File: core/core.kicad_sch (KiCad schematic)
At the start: 5 parts, among them U1 F1C200S, U2 EA3036C

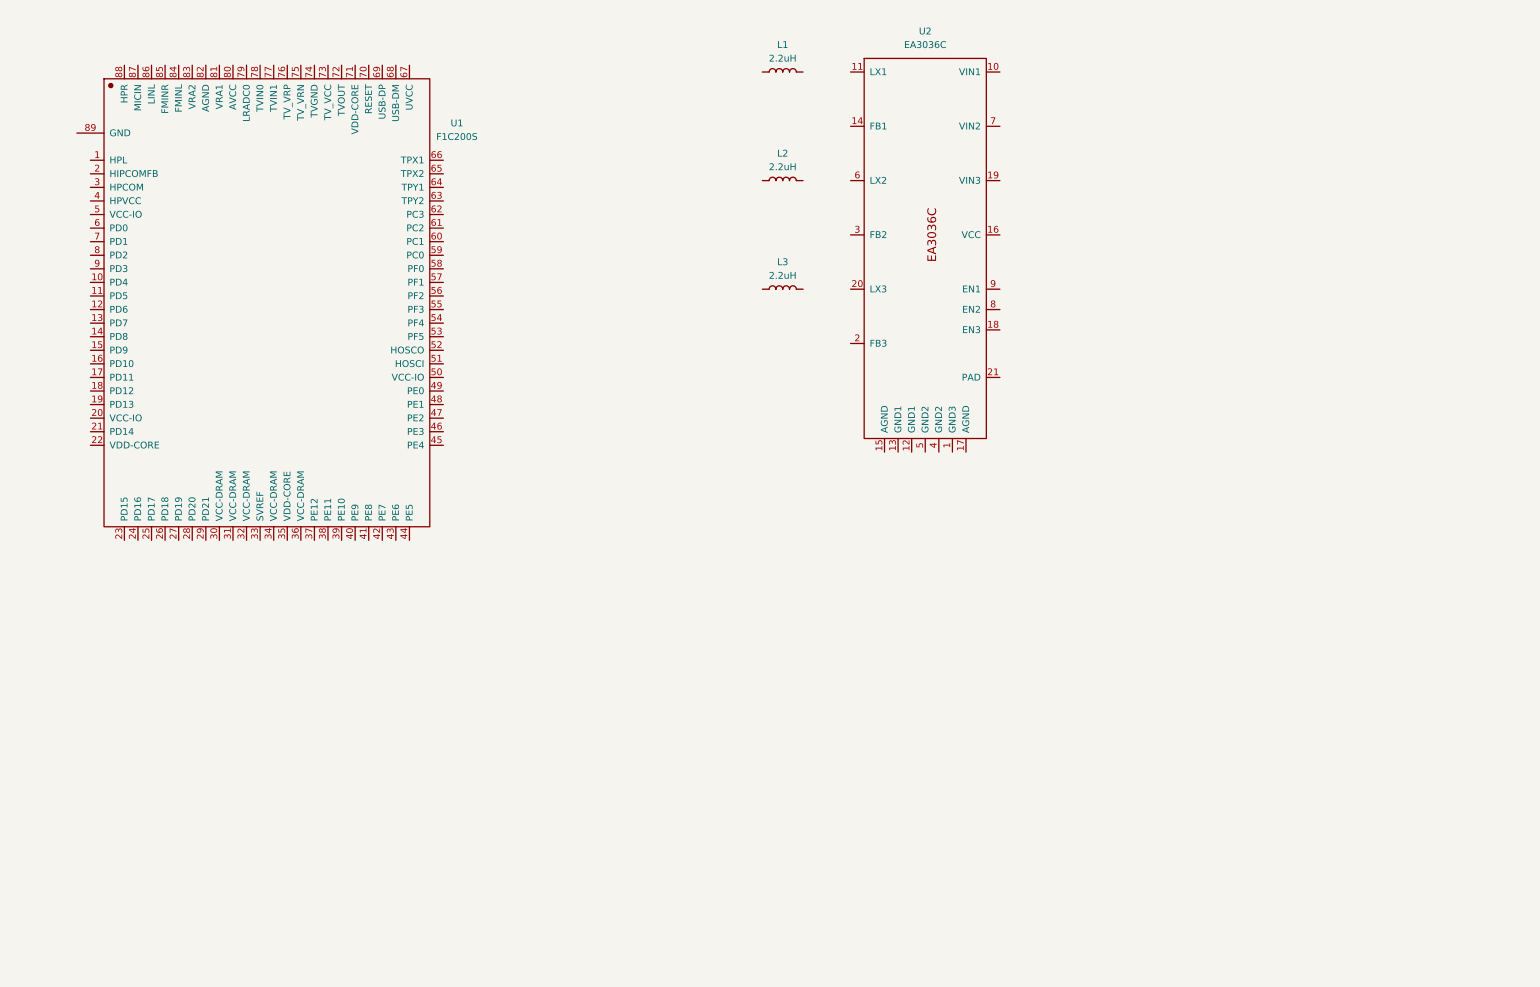
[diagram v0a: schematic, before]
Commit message: finish schemtic except soc
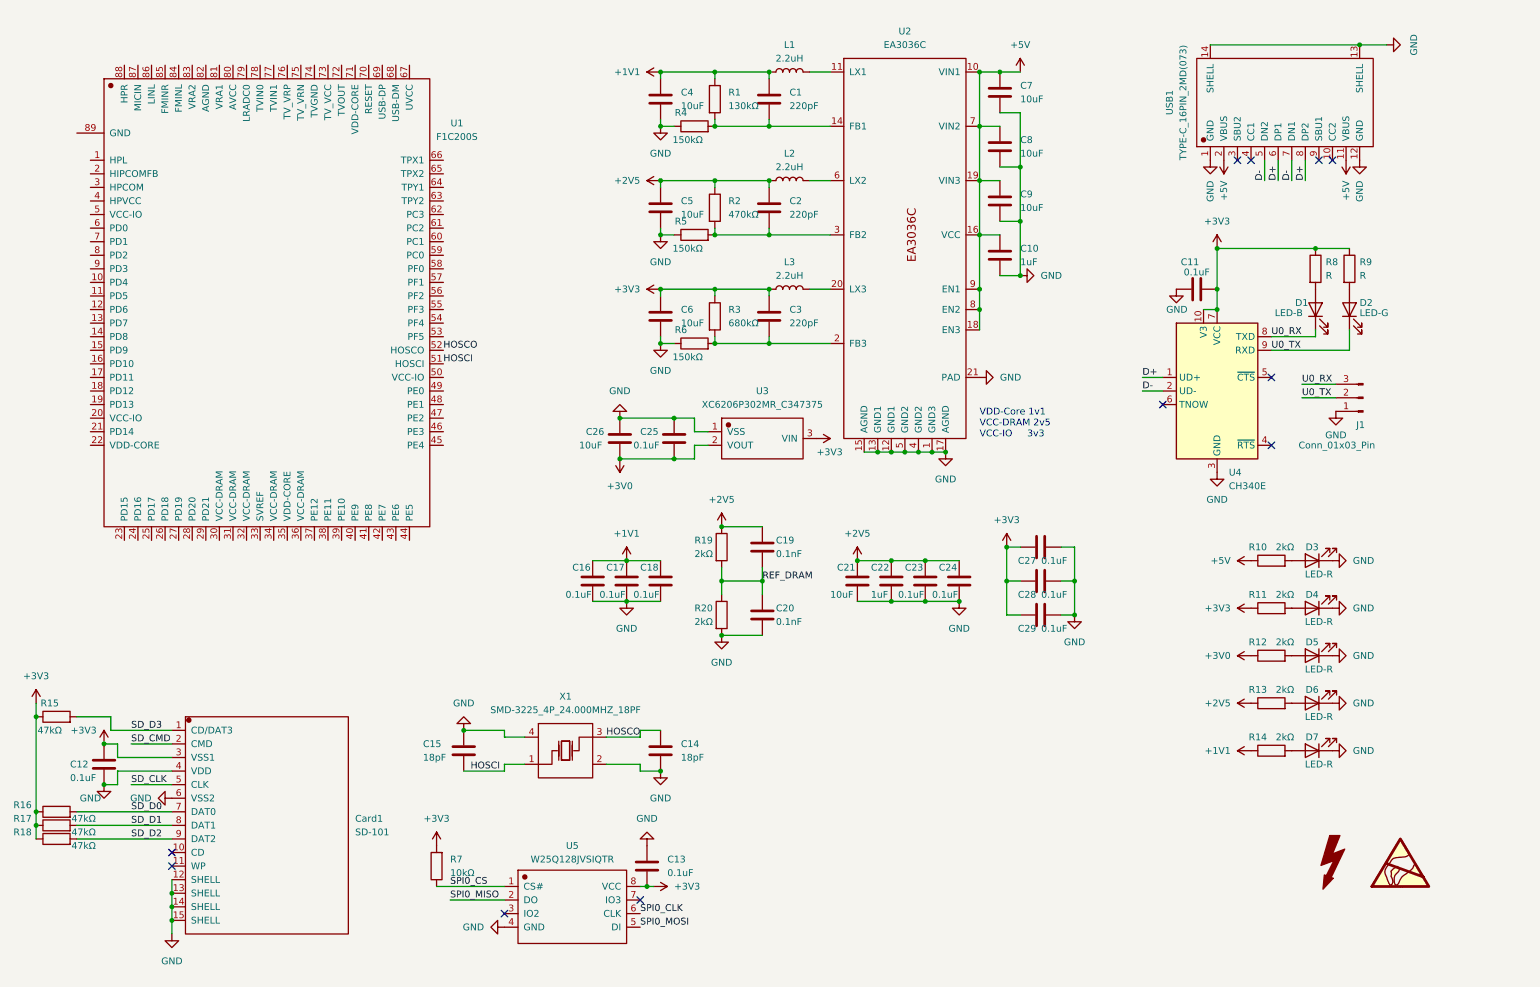
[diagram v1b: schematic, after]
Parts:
- added C1, C2, C3: 220pF, Capacitor_SMD:C_0603_1608Metric_Pad1.08x0.95mm_HandSolder, symbol Device:C
- added C10: 1uF, symbol Device:C
- added C11, C12, C13: 0.1uF, symbol Device:C
- added C14, C15: 18pF, symbol Device:C
- added C16, C17, C18, C23, C24, C25: 0.1uF, Capacitor_SMD:C_0603_1608Metric_Pad1.08x0.95mm_HandSolder, symbol Device:C
- added C19, C20: 0.1nF, Capacitor_SMD:C_0603_1608Metric_Pad1.08x0.95mm_HandSolder, symbol Device:C
- added C21, C26: 10uF, Capacitor_SMD:C_0603_1608Metric_Pad1.08x0.95mm_HandSolder, symbol Device:C
- added C22: 1uF, Capacitor_SMD:C_0603_1608Metric_Pad1.08x0.95mm_HandSolder, symbol Device:C
- added C27, C28, C29: 0.1uF, Capacitor_SMD:C_0603_1608Metric, symbol Device:C
- added C4, C5, C6: 10uF, Capacitor_SMD:C_0805_2012Metric_Pad1.18x1.45mm_HandSolder, symbol Device:C
- added C7, C8, C9: 10uF, symbol Device:C
- added Card1: SD-101, kicad_lceda:SD-SMD_SD-101, symbol kicad_lceda:SD-101
- added D1: LED-B, LED_SMD:LED_0603_1608Metric_Pad1.05x0.95mm_HandSolder, symbol Device:LED
- added D2: LED-G, LED_SMD:LED_0603_1608Metric_Pad1.05x0.95mm_HandSolder, symbol Device:LED
- added D3, D4, D5, D6, D7: LED-R, LED_SMD:LED_0603_1608Metric_Pad1.05x0.95mm_HandSolder, symbol Device:LED
- added J1: Conn_01x03_Pin, Connector_PinHeader_2.54mm:PinHeader_1x03_P2.54mm_Vertical, symbol Connector:Conn_01x03_Pin
- added R1: 130kΩ, Resistor_SMD:R_0201_0603Metric_Pad0.64x0.40mm_HandSolder, symbol Device:R
- added R10, R11, R12, R13, R14: 2kΩ, LED_SMD:LED_0603_1608Metric_Pad1.05x0.95mm_HandSolder, symbol Device:R
- added R15, R16, R17, R18: 47kΩ, Resistor_SMD:R_0603_1608Metric_Pad0.98x0.95mm_HandSolder, symbol Device:R
- added R19, R20: 2kΩ, Resistor_SMD:R_0603_1608Metric_Pad0.98x0.95mm_HandSolder, symbol Device:R
- added R2: 470kΩ, Resistor_SMD:R_0201_0603Metric_Pad0.64x0.40mm_HandSolder, symbol Device:R
- added R3: 680kΩ, Resistor_SMD:R_0201_0603Metric_Pad0.64x0.40mm_HandSolder, symbol Device:R
- added R4, R5, R6: 150kΩ, Resistor_SMD:R_0201_0603Metric_Pad0.64x0.40mm_HandSolder, symbol Device:R
- added R7: 10kΩ, symbol Device:R
- added R8, R9: R, symbol Device:R
- added U3: XC6206P302MR_C347375, kicad_lceda:SOT-23-3_L3.0-W1.7-P0.95-LS2.9-BR, symbol kicad_lceda:XC6206P302MR_C347375
- added U4: CH340E, Package_SO:MSOP-10_3x3mm_P0.5mm, symbol Interface_USB:CH340E
- added U5: W25Q128JVSIQTR, kicad_lceda:SOIC-8_L5.3-W5.3-P1.27-LS8.0-BL, symbol kicad_lceda:W25Q128JVSIQTR
- added USB1: TYPE-C_16PIN_2MD(073), kicad_lceda:USB-C-SMD_TYPE-C-6PIN-2MD-073, symbol kicad_lceda:TYPE-C_16PIN_2MD(073)
- added X1: SMD-3225_4P_24.000MHZ_18PF, kicad_lceda:CRYSTAL-SMD_4P-L3.2-W2.5-BL, symbol kicad_lceda:SMD-3225_4P_24.000MHZ_18PF
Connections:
- net GND: now reaches U2.1 (GND3)
- net GND: now also U2.12 (GND1), U2.13 (GND1), U2.15 (AGND), U2.17 (AGND), U2.21 (PAD), U2.4 (GND2), U2.5 (GND2), C10.2, C11.1, C12.1, C13.1, C14.2, C15.1, C16.2, C17.2, C18.2, C20.2, C21.2, C22.2, C23.2, C24.2, C25.1, C26.1, C27.2, C28.2, C29.2, C4.2, C5.2, C6.2, C7.2, C8.2, C9.2, Card1.12 (SHELL), Card1.13 (SHELL), Card1.14 (SHELL), Card1.15 (SHELL), Card1.4 (VDD), Card1.6 (VSS2), D3.1 (K), D4.1 (K), D5.1 (K), D6.1 (K), D7.1 (K), J1.1 (Pin_1), R20.2, R4.1, R5.1, R6.1, U3.1 (VSS), U4.3 (GND), U5.4 (GND), USB1.1 (GND), USB1.12 (GND), USB1.13 (SHELL), USB1.14 (SHELL), X1.2 (GND), X1.4 (GND)
- net +5V: now reaches U2.10 (VIN1)
- net +5V: now also U2.16 (VCC), U2.18 (EN3), U2.19 (VIN3), U2.7 (VIN2), U2.8 (EN2), U2.9 (EN1), C10.1, C7.1, C8.1, C9.1, R10.1, USB1.11 (VBUS), USB1.2 (VBUS)
- net at U2.11 (LX1): now also L1.2
- net at U2.14 (FB1): now also C1.2, R1.2, R4.2
- net at U2.2 (FB3): now also C3.2, R3.2, R6.2
- net at U2.20 (LX3): now also L3.2
- net at U2.3 (FB2): now also C2.2, R2.2, R5.2
- net at U2.6 (LX2): now also L2.2
- net +3V3: now reaches L3.1
- net +3V3: now also C11.2, C12.2, C13.2, C27.1, C28.1, C29.1, C3.1, C6.1, Card1.3 (VSS1), R11.1, R15.1, R16.1, R17.1, R18.1, R3.1, R7.2, R8.1, R9.1, U3.3 (VIN), U4.10 (V3), U4.7 (VCC), U5.8 (VCC)
- net +2V5: now reaches L2.1
- net +2V5: now also C19.1, C2.1, C21.1, C22.1, C23.1, C24.1, C5.1, R13.1, R19.1, R2.1
- net HOSCI: now reaches U1.51 (HOSCI)
- net HOSCI: now also C15.2, X1.1 (OSC1)
- net HOSCO: now reaches U1.52 (HOSCO)
- net HOSCO: now also C14.1, X1.3 (OSC2)
- net +1V1: now reaches L1.1
- net +1V1: now also C1.1, C16.1, C17.1, C18.1, C4.1, R1.1, R14.1
- new net: D2.2 (A), R9.2
- new net: D3.2 (A), R10.2
- new net: D5.2 (A), R12.2
- new net: D7.2 (A), R14.2
- new net: D1.2 (A), R8.2
- new net: D4.2 (A), R11.2
- new net: D6.2 (A), R13.2
- new net +3V0: C25.2, C26.2, R12.1, U3.2 (VOUT)
- new net D+: U4.1 (UD+), USB1.6 (DP1), USB1.8 (DP2)
- new net D-: U4.2 (UD-), USB1.5 (DN2), USB1.7 (DN1)
- new net REF_DRAM: C19.2, C20.1, R19.2, R20.1
- new net SD_CLK: Card1.5 (CLK)
- new net SD_CMD: Card1.2 (CMD)
- new net SD_D0: Card1.7 (DAT0), R16.2
- new net SD_D1: Card1.8 (DAT1), R17.2
- new net SD_D2: Card1.9 (DAT2), R18.2
- new net SD_D3: Card1.1 (CD/DAT3), R15.2
- new net SPI0_CLK: U5.6 (CLK)
- new net SPI0_CS: R7.1, U5.1 (CS#)
- new net SPI0_MISO: U5.2 (DO)
- new net SPI0_MOSI: U5.5 (DI)
- new net U0_RX: D1.1 (K), J1.3 (Pin_3), U4.8 (TXD)
- new net U0_TX: D2.1 (K), J1.2 (Pin_2), U4.9 (RXD)
- no-connect marks 0 -> 11
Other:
- note added: "VDD-Core 1v1 VCC-DRAM 2v5 VCC-IO 3v3"
- moved on the sheet: L1, L2, L3, U2

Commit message: finish core schematic
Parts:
- added C30, C31, C32: 0.1uF, Capacitor_SMD:C_0603_1608Metric_Pad1.08x0.95mm_HandSolder, symbol Device:C
- added D8: LED-R, LED_SMD:LED_0603_1608Metric_Pad1.05x0.95mm_HandSolder, symbol Device:LED
- added D9: LED-G, LED_SMD:LED_0603_1608Metric_Pad1.05x0.95mm_HandSolder, symbol Device:LED
- added J2: Conn_01x03_Pin, Connector_PinHeader_1.27mm:PinHeader_1x03_P1.27mm_Vertical, symbol Connector:Conn_01x03_Pin
- added LED1, LED2, LED3, LED4, LED5, LED6, LED7, LED8: WS2812B-2020, kicad_lceda:LED-SMD_4P-L2.0-W2.0-TL_WS2812B-2020, symbol kicad_lceda:WS2812B-2020
- added R21, R22, R23, R24: 5.1kΩ, Resistor_SMD:R_0603_1608Metric_Pad0.98x0.95mm_HandSolder, symbol Device:R
- added R25, R26: 2kΩ, Resistor_SMD:R_0603_1608Metric_Pad0.98x0.95mm_HandSolder, symbol Device:R
- added R27, R28, R29: 10kΩ, Resistor_SMD:R_0603_1608Metric_Pad0.98x0.95mm_HandSolder, symbol Device:R
- added SW1, SW2, SW3: DS-THAM04-ABB-R, kicad_lceda:SW-SMD_D-SWITCH_DS-THAM04-ABB-R, symbol kicad_lceda:DS-THAM04-ABB-R
- added USB2: TYPE-C_16PIN_2MD(073), kicad_lceda:USB-C-SMD_TYPE-C-6PIN-2MD-073, symbol kicad_lceda:TYPE-C_16PIN_2MD(073)
- C10, C11, C12, C13, C14, C15, C7, C8, C9: footprint (none) -> Capacitor_SMD:C_0603_1608Metric_Pad1.08x0.95mm_HandSolder
- C27, C28, C29: footprint Capacitor_SMD:C_0603_1608Metric -> Capacitor_SMD:C_0603_1608Metric_Pad1.08x0.95mm_HandSolder
- J1: footprint Connector_PinHeader_2.54mm:PinHeader_1x03_P2.54mm_Vertical -> Connector_PinHeader_1.27mm:PinHeader_1x03_P1.27mm_Vertical
- R1, R2, R3, R4, R5, R6: footprint Resistor_SMD:R_0201_0603Metric_Pad0.64x0.40mm_HandSolder -> Resistor_SMD:R_0603_1608Metric_Pad0.98x0.95mm_HandSolder
- R10, R11, R12, R13, R14: footprint LED_SMD:LED_0603_1608Metric_Pad1.05x0.95mm_HandSolder -> Resistor_SMD:R_0603_1608Metric_Pad0.98x0.95mm_HandSolder
- R7: footprint (none) -> Resistor_SMD:R_0603_1608Metric_Pad0.98x0.95mm_HandSolder
- R8, R9: value R -> 2kΩ; footprint (none) -> Resistor_SMD:R_0603_1608Metric_Pad0.98x0.95mm_HandSolder
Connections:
- net +1V1: now also U1.22 (VDD-CORE), U1.35 (VDD-CORE), U1.71 (VDD-CORE)
- net +2V5: now also U1.30 (VCC-DRAM), U1.31 (VCC-DRAM), U1.32 (VCC-DRAM), U1.34 (VCC-DRAM), U1.36 (VCC-DRAM)
- net +3V0: now also U1.80 (AVCC)
- net +3V3: now also U1.20 (VCC-IO), U1.4 (HPVCC), U1.5 (VCC-IO), U1.50 (VCC-IO), U1.67 (UVCC), U1.73 (TV_VCC), R25.1, R26.1, R27.2, R28.2, R29.2
- net +5V: now also LED1.4 (VDD), LED2.4 (VDD), LED3.4 (VDD), LED4.4 (VDD), LED5.4 (VDD), LED6.4 (VDD), LED7.4 (VDD), LED8.4 (VDD), USB2.11 (VBUS), USB2.2 (VBUS)
- net GND: now also U1.74 (TVGND), U1.82 (AGND), U1.89 (GND), C30.1, C31.1, C32.1, J2.1 (Pin_1), LED1.2 (GND), LED2.2 (GND), LED3.2 (GND), LED4.2 (GND), LED5.2 (GND), LED6.2 (GND), LED7.2 (GND), LED8.2 (GND), R21.2, R22.2, R23.2, R24.2, SW1.1, SW1.3, SW1.4, SW2.1, SW2.3, SW2.4, SW3.1, SW3.3, SW3.4, USB2.1 (GND), USB2.12 (GND), USB2.13 (SHELL), USB2.14 (SHELL)
- net REF_DRAM: now also U1.33 (SVREF)
- net SD_CLK: now also U1.56 (PF2)
- net SD_CMD: now also U1.55 (PF3)
- net SD_D0: now also U1.57 (PF1)
- net SD_D1: now also U1.58 (PF0)
- net SD_D2: now also U1.53 (PF5)
- net SD_D3: now also U1.54 (PF4)
- net SPI0_CLK: now also U1.59 (PC0)
- net SPI0_CS: now also U1.60 (PC1)
- net SPI0_MISO: now also U1.61 (PC2)
- net SPI0_MOSI: now also U1.62 (PC3)
- net U0_RX: now also U1.49 (PE0)
- net U0_TX: now also U1.48 (PE1)
- net at USB1.10 (CC2): now also R22.1
- net at USB1.4 (CC1): now also R21.1
- net U1_TX: now reaches U1.10 (PD4)
- net U1_TX: now also J2.2 (Pin_2)
- net SW0: now reaches U1.24 (PD16)
- net SW0: now also C31.2, R28.1, SW2.2
- net SW1: now reaches U1.25 (PD17)
- net SW1: now also C32.2, R29.1, SW3.2
- net WS0: now reaches U1.26 (PD18)
- net WS0: now also LED1.3 (DI)
- net WS1: now reaches U1.27 (PD19)
- net WS1: now also LED5.3 (DI)
- net LED0: now reaches U1.28 (PD20)
- net LED0: now also D8.1 (K)
- net LED1: now reaches U1.29 (PD21)
- net LED1: now also D9.1 (K)
- net BD-: now reaches U1.68 (USB-DM)
- net BD-: now also USB2.5 (DN2), USB2.7 (DN1)
- net BD+: now reaches U1.69 (USB-DP)
- net BD+: now also USB2.6 (DP1), USB2.8 (DP2)
- net RESET: now reaches U1.70 (RESET)
- net RESET: now also C30.2, R27.1, SW1.2
- net U1_RX: now reaches U1.9 (PD3)
- net U1_RX: now also J2.3 (Pin_3)
- new net: LED5.1 (DO), LED6.3 (DI)
- new net: LED2.1 (DO), LED3.3 (DI)
- new net: LED1.1 (DO), LED2.3 (DI)
- new net: LED6.1 (DO), LED7.3 (DI)
- new net: LED7.1 (DO), LED8.3 (DI)
- new net: R24.1, USB2.10 (CC2)
- new net: R23.1, USB2.4 (CC1)
- new net: D8.2 (A), R25.2
- new net: D9.2 (A), R26.2
- new net: LED3.1 (DO), LED4.3 (DI)
- no-connect marks 11 -> 58
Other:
- note added: "2023-09-02"
- note added: "Designed by Zhang-JK with 󱢠"
- note added: "Fragaria-Cake"
- note added: "Fragaria-Cake "
- note added: "Schematic of the Core"
- note added: "V-0.1"
- moved on the sheet: C1, C10, C11, C13, C14, C15, C16, C17, C18, C19, C2, C20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

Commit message: finish layout'
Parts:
- removed Card1: SD-101, kicad_lceda:SD-SMD_SD-101, symbol kicad_lceda:SD-101
- added Card2: MR01A-01211, kicad_lceda:TF-SMD_MR01A-01211, symbol kicad_lceda:MR01A-01211
- added U6: MPCIE-Socket, mpcie:mpcie-full-card, symbol mpcie:MPCIE-Socket
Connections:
- net +3V3: now also Card2.4 (VDD)
- net GND: now also Card2.10 (GND), Card2.11 (GND), Card2.12 (GND), Card2.13 (GND), Card2.6 (VSS)
- net LED0: now also U1.7 (PD1); no longer U1.28 (PD20)
- net LED1: now also U1.6 (PD0); no longer U1.29 (PD21)
- net SD_CLK: now also Card2.5 (CLK)
- net SD_CMD: now also Card2.3 (CMD)
- net SD_D0: now also R17.2, Card2.7 (DAT0); no longer R16.2
- net SD_D1: now also R18.2, Card2.8 (DAT1); no longer R17.2
- net SD_D2: now also R15.2, Card2.1 (DAT2); no longer R18.2
- net SD_D3: now also R16.2, Card2.2 (CD/DAT3); no longer R15.2
- net SW0: now also U1.12 (PD6); no longer U1.24 (PD16)
- net SW1: now also U1.13 (PD7); no longer U1.25 (PD17)
- net WS0: now also U1.11 (PD5); no longer U1.26 (PD18)
- net WS1: now also U1.14 (PD8); no longer U1.27 (PD19)
- no-connect marks 58 -> 105
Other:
- moved on the sheet: C11, C12, C13, C14, C15, C16, C17, C18, C19, C20, C21, C22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

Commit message: minor bug fix
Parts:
- C19, C20: value 0.1nF -> 0.1uF
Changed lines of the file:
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@@
       (effects (font (size 1.27 1.27)) (justify left))
     )
-    (property "Value" "0.1nF" (at 226.695 116.205 0)
+    (property "Value" "0.1uF" (at 226.695 116.205 0)
       (effects (font (size 1.27 1.27)) (justify left))
     )
@@
       (effects (font (size 1.27 1.27)) (justify left))
     )
-    (property "Value" "0.1nF" (at 226.695 128.905 0)
-      (effects (font (size 1.27 1.27)) (justify left))
-    )
+    (property "Value" "0.1uF" (at 226.695 128.905 0)
+      (effects (font (size 1.27 1.27)) (justify left))
+    )
